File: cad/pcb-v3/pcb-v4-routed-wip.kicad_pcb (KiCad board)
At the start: 4 copper layers, 19.3 x 19.3 mm, 50 parts

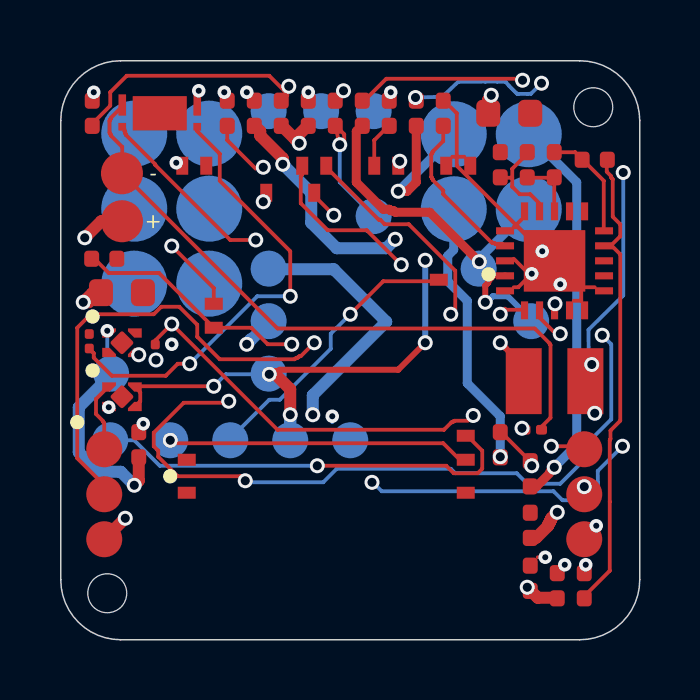
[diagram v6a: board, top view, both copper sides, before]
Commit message: Fine-pitch escape ring: U3/U4 get a reserved 0.55 mm ring; 3 blockers
Five of the ten open pads were on U3/U4, and the cause was structural: they are
TPS7A2033 in X2SON-4 with pads 0.34-0.40 mm apart, so nothing routes BETWEEN
their pins at 0.127/0.10 -- every pin must escape radially. R8 sat 1.11 mm to
one side, R9 1.09 mm to the other, TP6 directly above, C5 below. U4 was boxed
in on four sides.

The packer could not know. Worse, the elbow-room objective I added earlier
actively PREFERRED those spots, because the gap beside a fine-pitch part is the
emptiest-looking space on the board. FINE_PITCH/FINE_ESCAPE now reserves a
0.55 mm ring in _legal_mask, at the source, and the 0201 objective goes back to
nearest-U5 since it no longer has to carry a job that was never its own.

  open pads 10 -> 9, and stage 1 routes 9/9 with the pogo keep-outs in place

TWO SELF-INFLICTED BUGS FOUND AND FIXED ALONG THE WAY:

* The 0201 scoring ranked by distance WITHIN a rotation and by free space
  BETWEEN rotations. Two comparisons deciding the same thing, disagreeing --
  so the fix appeared to do nothing at all and R8 stayed 21.5 mm from U5.

* check_board.py flagged copper sitting EXACTLY on the 0.10 rule: shapely
  returns 0.09999999998 and  calls that a violation, printed as
  '0.1000'. The router's own check_drc passes the same board clean. Now
  compares against MIN_CU - 1e-6; a nanometre is below any fab resolution and
  well above float noise.

Also recorded a dead end: a hand-written dangling-segment remover deleted 334
of 593 segments because its 'is this end anchored' test knew about segments and
vias but FORGOT PADS. Tracks end on pads. Reverted; the board here is the
un-stitched route, which has 9 open pads but no stubs.
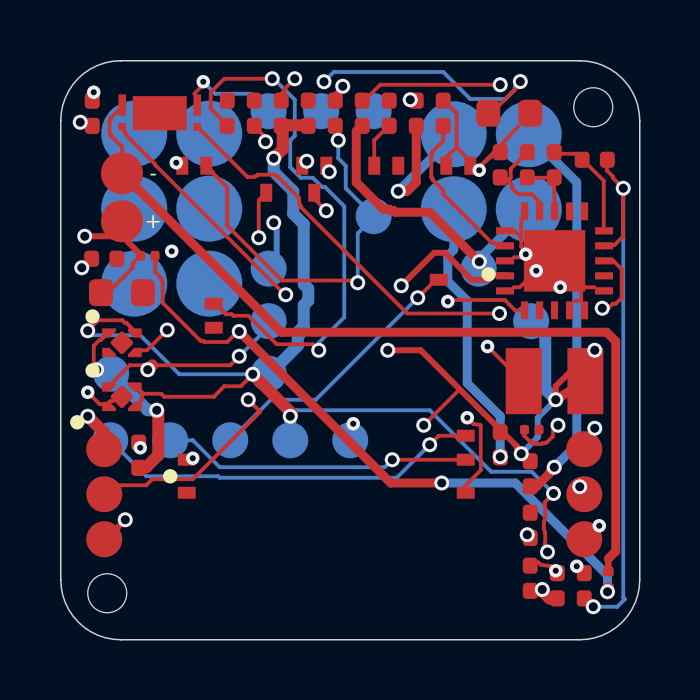
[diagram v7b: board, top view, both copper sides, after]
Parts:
- moved R9 15.0 mm to (6.05, 2.65), turned to 0 degrees
- moved C14 5.59 mm to (8.60, 7.65), turned to 90 degrees
- moved R8 3.21 mm to (-6.75, -3.15), turned to 0 degrees
- moved C8 0.35 mm to (-7.05, 3.50)
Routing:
- net VBAT: track 43.4 -> 12.4 mm, vias 7 -> 2
- net VBAT_OK: track 4.41 -> 29.5 mm, vias 1 -> 3
- net VSTOR: track 56.8 -> 41.3 mm, vias 9 -> 7
- net CELL_NEG: track 22.2 -> 29.2 mm
- net PCM_VDD: track 24.1 -> 31.0 mm
- net SENSOR_WAKEUP: track 20.9 -> 15.0 mm
- net BL_FLAG: track 56.7 -> 51.3 mm, vias 6 -> 3
- net GND: track 11.8 -> 16.8 mm, vias 18 -> 16
- net PCM_VM: track 15.2 -> 19.0 mm
- net SENSOR_3V3: track 28.0 -> 31.4 mm, vias 4 -> 6
- net OK_PROG: track 15.8 -> 18.9 mm, vias 0 -> 2
- net VBAT_SENSE: track 28.2 -> 25.4 mm, vias 2 -> 3
- net LX: track 3.75 -> 6.37 mm
- net VIN_DC: track 37.1 -> 39.7 mm
- net RESET: track 17.7 -> 19.6 mm
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
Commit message: Escape ring works: U3/U4 now fully connected; 2 blockers, both the fill
The 0.55 mm fine-pitch ring did what it was meant to. U3 and U4 -- five of the
ten open pads last round -- no longer appear in the disconnected list at all.
What remains is U1 (4 pads), U2 (2) and three GND passives.

Stitch closed six of those, then reported no improvement, because adding copper
STALES THE ZONE FILL: check_connected models the fill from the file, and the
new GND vias are not in it until KiCad re-fills. The count is pessimistic until
then, not wrong.

Removed a 2-segment floating GND stub on B.Cu that gnd_taps left behind -- a
1.2 mm chain stopping 0.25 mm short of C6.2, anchored at neither end. Removed
it by looping on PREFLIGHT'S OWN report rather than my own definition of
'dangling', after my hand-written version deleted 334 of 593 segments earlier
by forgetting that tracks end on pads. Two iterations, two segments, check 20
clean.

Passing: clearance, netlist (134 pins), router DRC, antenna keep-out, dangling
ends, sourcing, and no via through a pogo contact (84 vias vs 10 pads).
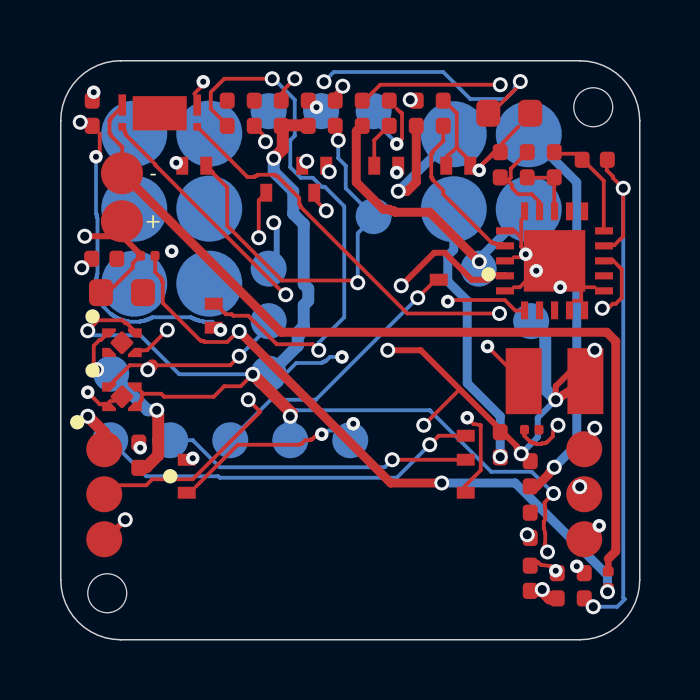
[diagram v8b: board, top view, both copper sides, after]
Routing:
- net None: track 0.00 -> 44.9 mm, vias 0 -> 7
- net GND: track 16.8 -> 15.0 mm
